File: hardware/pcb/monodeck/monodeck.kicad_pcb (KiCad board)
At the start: 2 copper layers, 72 x 54.8 mm, 15 parts, among them J1 Conn_01x20_Socket, J2 Conn_01x20_Socket, U1 TP4056

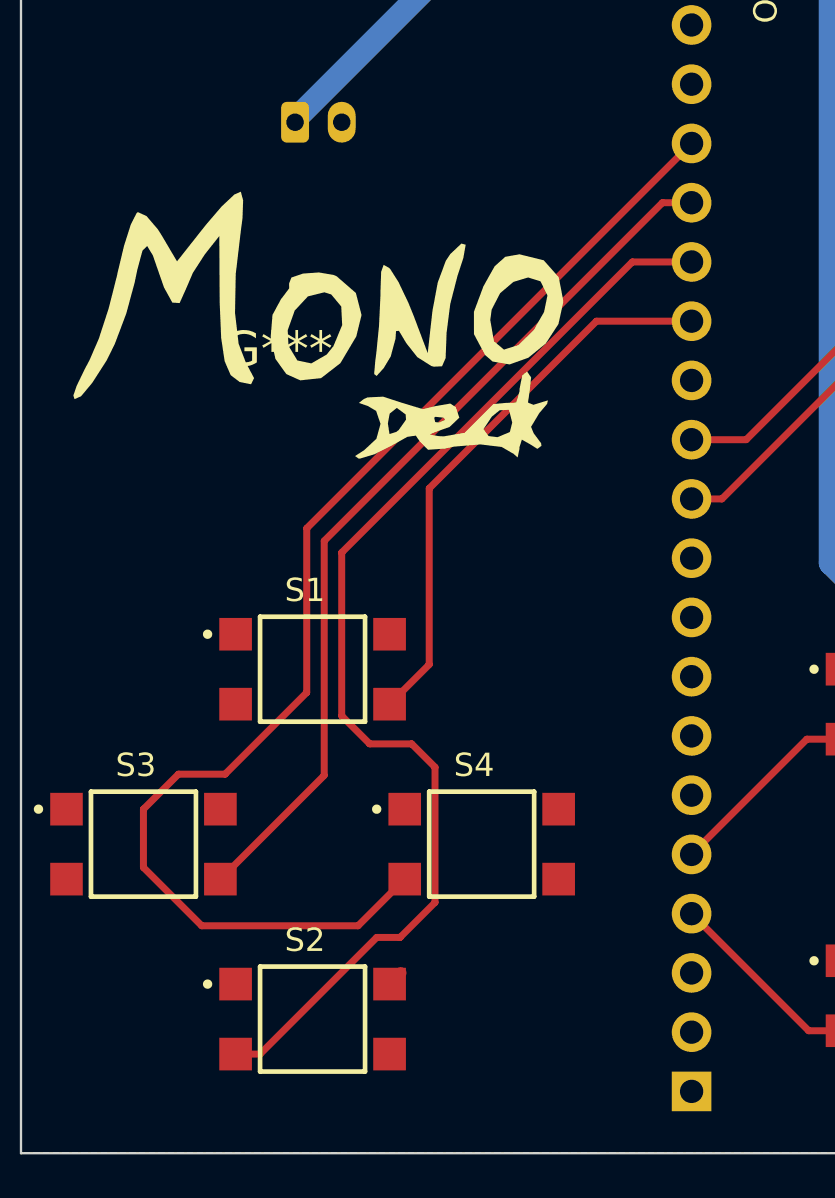
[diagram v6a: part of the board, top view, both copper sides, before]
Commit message: updated pcb and dpad pin mapping for efficient routing
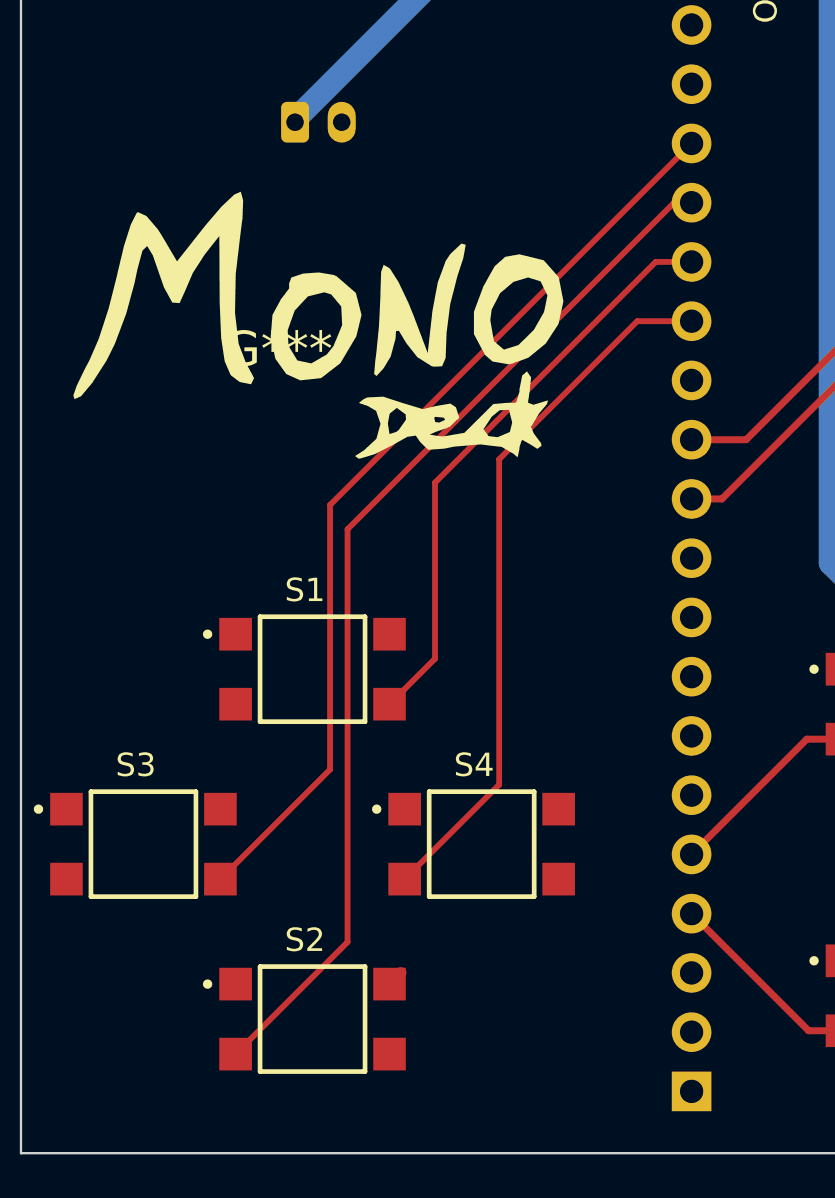
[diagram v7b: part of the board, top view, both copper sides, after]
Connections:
- S1 pad 4: /GPIO10 -> /GPIO11
- S2 pad 3: /GPIO11 -> /GPIO12
- S3 pad 4: /GPIO12 -> /GPIO13
- S4 pad 3: /GPIO13 -> /GPIO10
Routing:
- net /GPIO11: track 49.1 -> 25.2 mm
- net /GPIO13: track 55.0 -> 39.9 mm
- net /GPIO12: track 38.1 -> 45.0 mm
- net /GPIO10: track 24.2 -> 30.4 mm
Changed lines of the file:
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@@
 		(35 "F.Fab" user)
 		(33 "B.Fab" user)
-		(39 "User.1" user)
-		(41 "User.2" user)
-		(43 "User.3" user)
-		(45 "User.4" user)
 	)
 	(setup
+		(stackup
+			(layer "F.SilkS"
+				(type "Top Silk Screen")
+			)
+			(layer "F.Paste"
+				(type "Top Solder Paste")
+			)
+			(layer "F.Mask"
+				(type "Top Solder Mask")
+				(thickness 0.01)
+			)
+			(layer "F.Cu"
+				(type "copper")
+				(thickness 0.035)
+			)
+			(layer "dielectric 1"
+				(type "core")
+				(thickness 1.51)
+				(material "FR4")
+				(epsilon_r 4.5)
+				(loss_tangent 0.02)
+			)
+			(layer "B.Cu"
+				(type "copper")
+				(thickness 0.035)
+			)
+			(layer "B.Mask"
+				(type "Bottom Solder Mask")
+				(thickness 0.01)
+			)
+			(layer "B.Paste"
+				(type "Bottom Solder Paste")
+			)
+			(layer "B.SilkS"
+				(type "Bottom Silk Screen")
+			)
+			(copper_finish "None")
+			(dielectric_constraints no)
+		)
 		(pad_to_mask_clearance 0)
 		(allow_soldermask_bridges_in_footprints no)
@@
 			(size 1.4 1.4)
 			(layers "F.Cu" "F.Mask" "F.Paste")
-			(net 2 "/GPIO10")
+			(net 13 "/GPIO11")
 			(pintype "passive")
 			(solder_mask_margin 0.102)
@@
 			(size 1.4 1.4)
 			(layers "F.Cu" "F.Mask" "F.Paste")
-			(net 4 "/GPIO13")
+			(net 2 "/GPIO10")
 			(pintype "passive")
 			(solder_mask_margin 0.102)
@@
 			(size 1.4 1.4)
 			(layers "F.Cu" "F.Mask" "F.Paste")
-			(net 3 "/GPIO12")
+			(net 4 "/GPIO13")
 			(pintype "passive")
 			(solder_mask_margin 0.102)
@@
 			(size 1.4 1.4)
 			(layers "F.Cu" "F.Mask" "F.Paste")
-			(net 13 "/GPIO11")
+			(net 3 "/GPIO12")
 			(pintype "passive")
 			(solder_mask_margin 0.102)
@@
 	)
 	(segment
-		(start 144.55 86.5)
-		(end 146.251 84.799)
-		(width 0.3)
-		(layer "F.Cu")
-		(net 2)
-	)
-	(segment
-		(start 153.42 70.08)
+		(start 155.17 70.08)
 		(end 157.5 70.08)
-		(width 0.3)
+		(width 0.25)
 		(layer "F.Cu")
 		(net 2)
 	)
 	(segment
-		(start 146.251 77.249)
-		(end 153.42 70.08)
-		(width 0.3)
+		(start 149.25 76)
+		(end 155.17 70.08)
+		(width 0.25)
 		(layer "F.Cu")
 		(net 2)
 	)
 	(segment
-		(start 146.251 84.799)
-		(end 146.251 77.249)
-		(width 0.3)
+		(start 145.2 94)
+		(end 149.25 89.95)
+		(width 0.25)
 		(layer "F.Cu")
 		(net 2)
 	)
 	(segment
-		(start 141.75 79.5)
-		(end 156.25 65)
-		(width 0.3)
+		(start 149.25 89.95)
+		(end 149.25 76)
+		(width 0.25)
 		(layer "F.Cu")
-		(net 3)
+		(net 2)
 	)
 	(segment
-		(start 156.25 65)
+		(start 156.75 65)
 		(end 157.5 65)
-		(width 0.3)
+		(width 0.25)
 		(layer "F.Cu")
 		(net 3)
 	)
 	(segment
-		(start 137.3 94)
-		(end 141.75 89.55)
-		(width 0.3)
+		(start 142.75 96.7)
+		(end 142.75 79)
+		(width 0.25)
 		(layer "F.Cu")
 		(net 3)
 	)
 	(segment
-		(start 141.75 89.55)
-		(end 141.75 79.5)
-		(width 0.3)
+		(start 137.95 101.5)
+		(end 142.75 96.7)
+		(width 0.25)
 		(layer "F.Cu")
 		(net 3)
 	)
 	(segment
-		(start 141 86)
-		(end 141 78.96)
-		(width 0.3)
-		(layer "F.Cu")
-		(net 4)
-	)
-	(segment
-		(start 135.5 89.5)
-		(end 137.5 89.5)
-		(width 0.3)
-		(layer "F.Cu")
-		(net 4)
-	)
-	(segment
-		(start 137.5 89.5)
-		(end 141 86)
-		(width 0.3)
+		(start 142.75 79)
+		(end 156.75 65)
+		(width 0.25)
 		(layer "F.Cu")
-		(net 4)
+		(net 3)
 	)
 	(segment
-		(start 141 78.96)
+		(start 142 77.96)
 		(end 157.5 62.46)
-		(width 0.3)
-		(layer "F.Cu")
-		(net 4)
-	)
-	(segment
-		(start 136.5 96)
-		(end 134 93.5)
-		(width 0.3)
-		(layer "F.Cu")
-		(net 4)
-	)
-	(segment
-		(start 134 93.5)
-		(end 134 91)
-		(width 0.3)
-		(layer "F.Cu")
-		(net 4)
-	)
-	(segment
-		(start 134 91)
-		(end 135.5 89.5)
-		(width 0.3)
+		(width 0.25)
 		(layer "F.Cu")
 		(net 4)
 	)
 	(segment
-		(start 143.2 96)
-		(end 136.5 96)
-		(width 0.3)
+		(start 137.3 94)
+		(end 142 89.3)
+		(width 0.25)
 		(layer "F.Cu")
 		(net 4)
 	)
 	(segment
-		(start 145.2 94)
-		(end 143.2 96)
-		(width 0.3)
+		(start 142 89.3)
+		(end 142 77.96)
+		(width 0.25)
 		(layer "F.Cu")
 		(net 4)
@@
 	)
 	(segment
-		(start 142.5 80)
-		(end 154.96 67.54)
-		(width 0.3)
-		(layer "F.Cu")
-		(net 13)
-	)
-	(segment
-		(start 145 96.5)
-		(end 146.5 95)
-		(width 0.3)
-		(layer "F.Cu")
-		(net 13)
-	)
-	(segment
-		(start 143.701 88.201)
-		(end 142.5 87)
-		(width 0.3)
-		(layer "F.Cu")
-		(net 13)
-	)
-	(segment
-		(start 137.95 101.5)
-		(end 139 101.5)
-		(width 0.3)
-		(layer "F.Cu")
-		(net 13)
-	)
-	(segment
-		(start 139 101.5)
-		(end 144 96.5)
-		(width 0.3)
-		(layer "F.Cu")
-		(net 13)
-	)
-	(segment
-		(start 144 96.5)
-		(end 145 96.5)
-		(width 0.3)
-		(layer "F.Cu")
-		(net 13)
-	)
-	(segment
-		(start 146.5 89.201)
-		(end 145.5 88.201)
-		(width 0.3)
-		(layer "F.Cu")
-		(net 13)
-	)
-	(segment
-		(start 154.96 67.54)
+		(start 155.96 67.54)
 		(end 157.5 67.54)
-		(width 0.3)
+		(width 0.25)
 		(layer "F.Cu")
 		(net 13)
 	)
 	(segment
-		(start 142.5 87)
-		(end 142.5 80)
-		(width 0.3)
+		(start 146.5 84.55)
+		(end 146.5 77)
+		(width 0.25)
 		(layer "F.Cu")
 		(net 13)
 	)
 	(segment
-		(start 145.5 88.201)
-		(end 143.701 88.201)
-		(width 0.3)
+		(start 146.5 77)
+		(end 155.96 67.54)
+		(width 0.25)
 		(layer "F.Cu")
 		(net 13)
 	)
 	(segment
-		(start 146.5 95)
-		(end 146.5 89.201)
-		(width 0.3)
+		(start 144.55 86.5)
+		(end 146.5 84.55)
+		(width 0.25)
 		(layer "F.Cu")
 		(net 13)

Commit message: generated drill and gerber files
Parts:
- moved G*** 0.71 mm to (139.8, 72.0)
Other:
- board size 72 x 54.8 mm -> 72.5 x 54.8 mm
- board text added: "v2.3.0"
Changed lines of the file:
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@@
 		(tenting front back)
 		(pcbplotparams
-			(layerselection 0x00000000_00000000_55555555_5755f5ff)
+			(layerselection 0x00000000_00000000_5555555f_575555ff)
 			(plot_on_all_layers_selection 0x00000000_00000000_00000000_00000000)
 			(disableapertmacros no)
-			(usegerberextensions no)
+			(usegerberextensions yes)
 			(usegerberattributes yes)
 			(usegerberadvancedattributes yes)
@@
 			(sketchdnponfab yes)
 			(crossoutdnponfab yes)
-			(subtractmaskfromsilk no)
+			(subtractmaskfromsilk yes)
 			(outputformat 1)
 			(mirror no)
-			(drillshape 1)
+			(drillshape 0)
 			(scaleselection 1)
-			(outputdirectory "")
+			(outputdirectory "/home/dakshesh/MonoDeck/hardware/pcb/gerbers/")
 		)
 	)
@@
 	(footprint "LOGO"
 		(layer "F.Cu")
-		(at 139.77531 71.290622)
+		(at 139.77531 72)
 		(property "Reference" "G***"
 			(at 0 0 0)
 			(layer "F.SilkS")
+			(hide yes)
 			(effects
 				(font
@@
 				(font
 					(size 1 1)
-					(thickness 0.1)
+					(thickness 0.15)
 				)
 				(justify mirror)
@@
 		(tags "Through hole socket strip THT 1x20 2.54mm single row")
 		(property "Reference" "J1"
-			(at 0 2.77 0)
+			(at 2.794 0.508 270)
 			(layer "B.SilkS")
 			(effects
@@
 		)
 		(property "Value" "Conn_01x20_Socket"
-			(at 0 -51.03 0)
+			(at 0 -51.03 180)
 			(layer "B.Fab")
 			(effects
@@
 		)
 		(property "Datasheet" "~"
-			(at 0 0 0)
+			(at 0 0 180)
 			(layer "B.Fab")
 			(hide yes)
@@
 		)
 		(property "Description" "Generic connector, single row, 01x20, script generated"
-			(at 0 0 0)
+			(at 0 0 180)
 			(layer "B.Fab")
 			(hide yes)
@@
 		)
 		(fp_text user "${REFERENCE}"
-			(at 0 -24.13 90)
+			(at 0 -24.13 270)
 			(layer "B.Fab")
 			(effects
@@
 	(gr_rect
 		(start 128.75 51)
-		(end 200.75 105.75)
+		(end 201.25 105.75)
 		(stroke
 			(width 0.1)
@@
 		)
 	)
+	(gr_text "v2.3.0"
+		(at 150.5 78 0)
+		(layer "F.SilkS")
+		(effects
+			(font
+				(size 1 1)
+				(thickness 0.15)
+			)
+			(justify left bottom)
+		)
+	)
 	(segment
 		(start 144.55 98.5)
@@
 		(net_name "GND")
 		(layers "F.Cu" "B.Cu")
+		(name "GND")
 		(hatch edge 0.5)
 		(connect_pads
@@
 		(polygon
 			(pts
-				(xy 128.75 51) (xy 200.75 51) (xy 200.75 105.75) (xy 128.75 105.75)
+				(xy 128.75 51) (xy 201.25 51) (xy 201.25 105.75) (xy 128.75 105.75)
 			)
 		)
